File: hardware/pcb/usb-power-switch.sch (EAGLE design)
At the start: 15 parts, among them IC1 TPS2024, IC2 LD1117V33

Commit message: Updated PCB to v3
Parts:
- removed C5: 10uF, rcl:C-US025-025X050
- removed IC2: LD1117V33, SparkFun-PowerIC:V_REG_LD1117VXX
- removed R3, R4, R5: 10K, rcl:R-US_0207/10
- added C1: 22uF, rcl:C-US025-025X050
- added R1: 10K, rcl:R-US_0207/10
- added U2: LD1117V33, my-custom:LD1117
- C3: value 22uF -> 0.1uF
- C4: value 0.1uF -> 10uF
- IN: value USB-MINI-B -> WM17115-ND
- J1: value ESP-01 -> ESP8266-01
- OUT: value USB-A -> UE27AC54100-ND
- S1: value TACTILE-BUTTON-MJTP1230 -> MJTP1230
- renumbered IC1 to U1, JP1 to J1, JP2 to J2
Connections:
- removed net CH_PD: J1.3, R4.1
- removed net D+: IN.D+, OUT.D+
- removed net D-: IN.D-, OUT.D-
- removed net GPIO0: J1.6, R3.1, S1.1
- removed net RST: J1.5, R5.1
- new net PU: J1.3, J1.5, J1.6, R2.1, S1.1
- net /EN: now also R1.1; no longer R2.1
- net GND: now also C1.2, U2.GND; no longer C3.2, C5.2, IC2.GND
- net VCC: now also C4.1, R1.2, U2.VOUT; no longer C5.1, IC2.OUT, R3.2, R4.2, R5.2
- net VIN: now also C3.1, U2.VIN; no longer C4.1, IC2.IN
- net VOUT: now also C1.1; no longer C3.1
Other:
- moved on the sheet: C3, C4, IN, OUT, R2

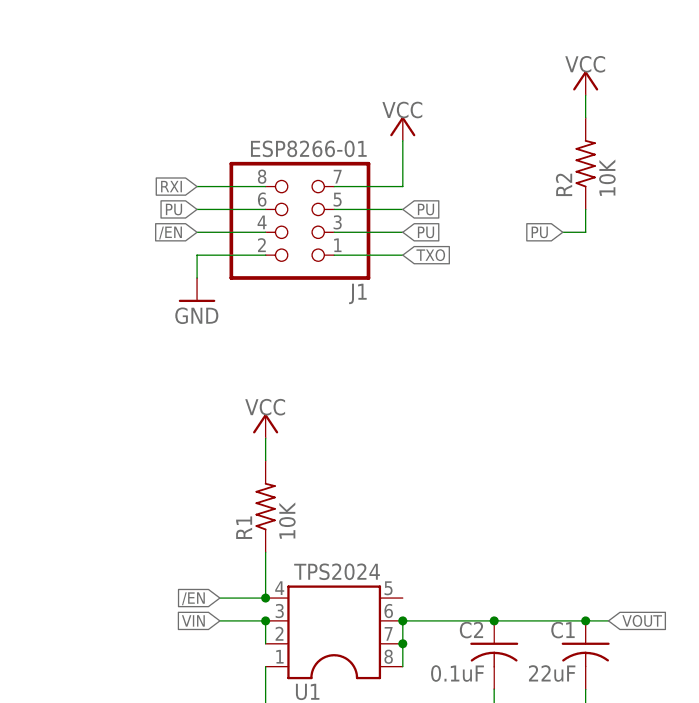
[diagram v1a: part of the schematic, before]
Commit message: Optimized routing, added repo URL
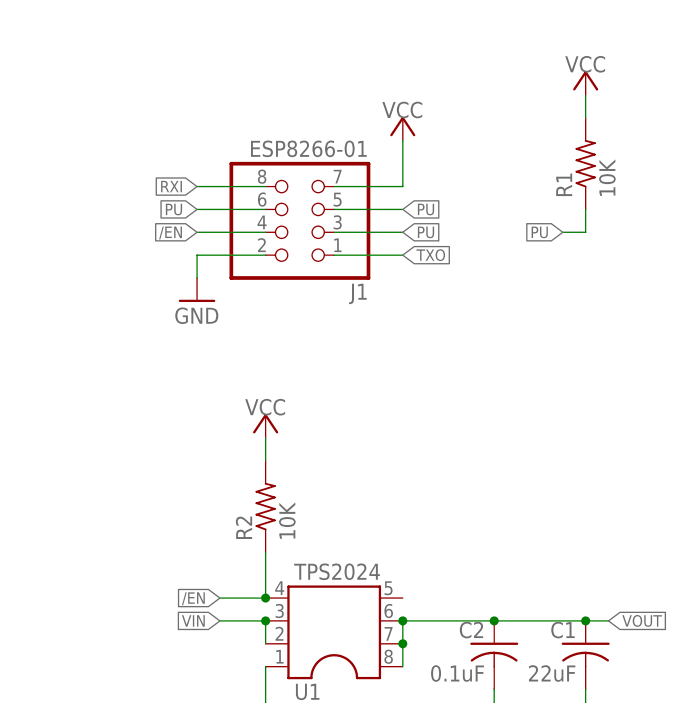
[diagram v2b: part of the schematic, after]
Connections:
- net /EN: now also R2.1; no longer R1.1
- net PU: now also R1.1; no longer R2.1
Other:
- moved on the sheet: R1, R2
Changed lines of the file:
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@@
 <part name="S1" library="my-custom" deviceset="TACTILE-BUTTON-MJTP1230" device="" value="MJTP1230"/>
 <part name="GND2" library="supply1" deviceset="GND" device=""/>
-<part name="R2" library="rcl" deviceset="R-US_" device="0207/10" value="10K"/>
+<part name="R1" library="rcl" deviceset="R-US_" device="0207/10" value="10K"/>
 <part name="U2" library="my-custom" deviceset="LD1117" device="" value="LD1117V33"/>
 <part name="GND3" library="supply1" deviceset="GND" device=""/>
@@
 <part name="J2" library="pinhead" deviceset="PINHD-1X6" device="" value="FTDI 3.3V"/>
 <part name="GND6" library="supply1" deviceset="GND" device=""/>
-<part name="R1" library="rcl" deviceset="R-US_" device="0207/10" value="10K"/>
+<part name="R2" library="rcl" deviceset="R-US_" device="0207/10" value="10K"/>
 <part name="P+2" library="supply1" deviceset="VCC" device=""/>
 <part name="P+4" library="supply1" deviceset="VCC" device=""/>
@@
 <instance part="S1" gate="G$1" x="182.88" y="137.16"/>
 <instance part="GND2" gate="1" x="195.58" y="134.62"/>
-<instance part="R2" gate="G$1" x="198.12" y="106.68" rot="R90"/>
+<instance part="R1" gate="G$1" x="198.12" y="106.68" rot="R90"/>
 <instance part="U2" gate="G$1" x="86.36" y="146.05"/>
 <instance part="GND3" gate="1" x="86.36" y="134.62"/>
@@
 </instance>
 <instance part="GND6" gate="1" x="83.82" y="88.9" rot="MR0"/>
-<instance part="R1" gate="G$1" x="162.56" y="68.58" rot="R90"/>
+<instance part="R2" gate="G$1" x="162.56" y="68.58" rot="R90"/>
 <instance part="P+2" gate="VCC" x="104.14" y="152.4" smashed="yes">
 <attribute name="VALUE" x="104.14" y="152.4" size="1.778" layer="96" rot="MR0" align="bottom-center"/>
@@
 <net name="VCC" class="0">
 <segment>
-<pinref part="R2" gate="G$1" pin="2"/>
+<pinref part="R1" gate="G$1" pin="2"/>
 <wire x1="198.12" y1="111.76" x2="198.12" y2="114.3" width="0.1524" layer="91"/>
 <pinref part="P+4" gate="VCC" pin="VCC"/>
@@
 <segment>
 <pinref part="P+7" gate="VCC" pin="VCC"/>
-<pinref part="R1" gate="G$1" pin="2"/>
+<pinref part="R2" gate="G$1" pin="2"/>
 <wire x1="162.56" y1="76.2" x2="162.56" y2="73.66" width="0.1524" layer="91"/>
 </segment>
@@
 </segment>
 <segment>
-<pinref part="R2" gate="G$1" pin="1"/>
+<pinref part="R1" gate="G$1" pin="1"/>
 <wire x1="198.12" y1="101.6" x2="198.12" y2="99.06" width="0.1524" layer="91"/>
 <wire x1="198.12" y1="99.06" x2="195.58" y2="99.06" width="0.1524" layer="91"/>
@@
 <pinref part="U1" gate="G$1" pin="4"/>
 <wire x1="162.56" y1="58.42" x2="157.48" y2="58.42" width="0.1524" layer="91"/>
-<pinref part="R1" gate="G$1" pin="1"/>
+<pinref part="R2" gate="G$1" pin="1"/>
 <wire x1="162.56" y1="63.5" x2="162.56" y2="58.42" width="0.1524" layer="91"/>
 <junction x="162.56" y="58.42"/>
